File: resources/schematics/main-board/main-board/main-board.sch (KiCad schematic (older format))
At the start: 11 parts, among them J1 Conn_01x02_Female, J2 Conn_01x04_Female, J3 Conn_01x04_Female, SW1 Switch_DPDT_7x7mm, SW2 SW_Push_45deg, SW3 SW_Push_45deg

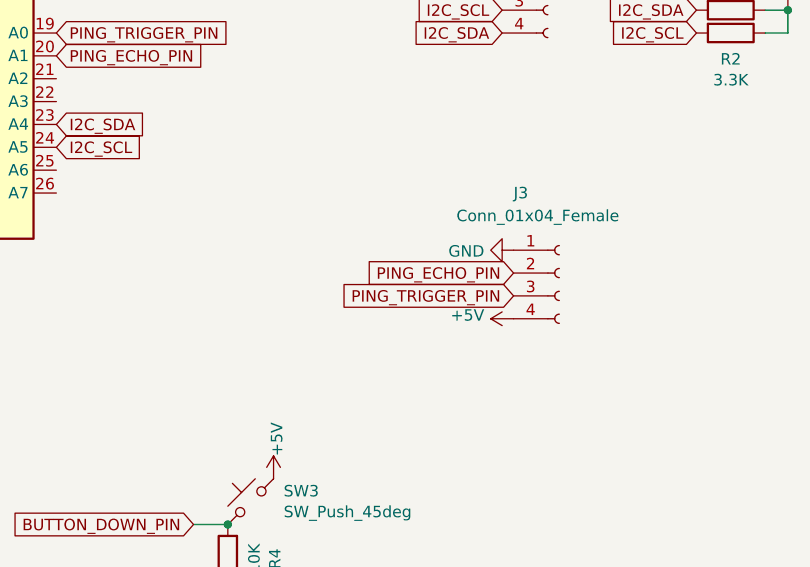
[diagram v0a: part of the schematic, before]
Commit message: Add horizontal pin header for connector
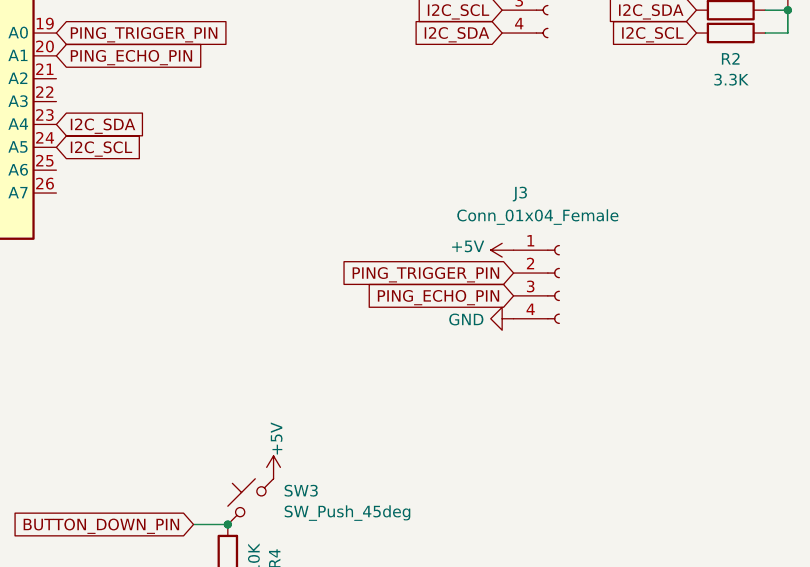
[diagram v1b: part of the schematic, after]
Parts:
- J3: footprint digikey-footprints:PinHeader_1x4_P2.54mm_Drill1.02mm -> Connector_PinHeader_2.54mm:PinHeader_1x04_P2.54mm_Horizontal
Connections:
- net +5V: now also J3.1 (Pin_1); no longer J3.4 (Pin_4)
- net GND: now also J3.4 (Pin_4); no longer J3.1 (Pin_1)
- net PING_ECHO_PIN: now also J3.3 (Pin_3); no longer J3.2 (Pin_2)
- net PING_TRIGGER_PIN: now also J3.2 (Pin_2); no longer J3.3 (Pin_3)
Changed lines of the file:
@@
 Text GLabel 5950 3100 0    50   Input ~ 0
 I2C_SDA
-$Comp
-L power:GND #PWR0106
-U 1 1 5E344AA7
-P 6000 4050
-F 0 "#PWR0106" H 6000 3800 50  0001 C CNN
-F 1 "GND" V 6005 3922 50  0000 R CNN
-F 2 "" H 6000 4050 50  0001 C CNN
-F 3 "" H 6000 4050 50  0001 C CNN
-	1    6000 4050
-	0    1    1    0
-$EndComp
-$Comp
-L power:+5V #PWR0107
-U 1 1 5E344D16
-P 6000 4350
-F 0 "#PWR0107" H 6000 4200 50  0001 C CNN
-F 1 "+5V" V 6015 4478 50  0000 L CNN
-F 2 "" H 6000 4350 50  0001 C CNN
-F 3 "" H 6000 4350 50  0001 C CNN
-	1    6000 4350
-	0    -1   -1   0
-$EndComp
-Text GLabel 6000 4250 0    50   Input ~ 0
+Text GLabel 6000 4150 0    50   Input ~ 0
 PING_TRIGGER_PIN
 $Comp
@@
 F 0 "J3" H 6000 4500 50  0000 L CNN
 F 1 "Conn_01x04_Female" H 5750 4400 50  0000 L CNN
-F 2 "digikey-footprints:PinHeader_1x4_P2.54mm_Drill1.02mm" H 6200 4150 50  0001 C CNN
+F 2 "Connector_PinHeader_2.54mm:PinHeader_1x04_P2.54mm_Horizontal" H 6200 4150 50  0001 C CNN
 F 3 "~" H 6200 4150 50  0001 C CNN
 	1    6200 4150
 	1    0    0    -1
 $EndComp
-Text GLabel 6000 4150 0    50   Input ~ 0
+Text GLabel 6000 4250 0    50   Input ~ 0
 PING_ECHO_PIN
 Wire Wire Line
@@
 Wire Wire Line
 	6200 1900 6050 1900
+$Comp
+L power:+5V #PWR0107
+U 1 1 5E344D16
+P 6000 4050
+F 0 "#PWR0107" H 6000 3900 50  0001 C CNN
+F 1 "+5V" V 6015 4178 50  0000 L CNN
+F 2 "" H 6000 4050 50  0001 C CNN
+F 3 "" H 6000 4050 50  0001 C CNN
+	1    6000 4050
+	0    -1   -1   0
+$EndComp
+$Comp
+L power:GND #PWR0106
+U 1 1 5E344AA7
+P 6000 4350
+F 0 "#PWR0106" H 6000 4100 50  0001 C CNN
+F 1 "GND" V 6005 4222 50  0000 R CNN
+F 2 "" H 6000 4350 50  0001 C CNN
+F 3 "" H 6000 4350 50  0001 C CNN
+	1    6000 4350
+	0    1    1    0
+$EndComp
 $EndSCHEMATC
